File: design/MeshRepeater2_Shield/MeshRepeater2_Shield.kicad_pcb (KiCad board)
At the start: 2 copper layers, 90 x 60 mm, 5 parts

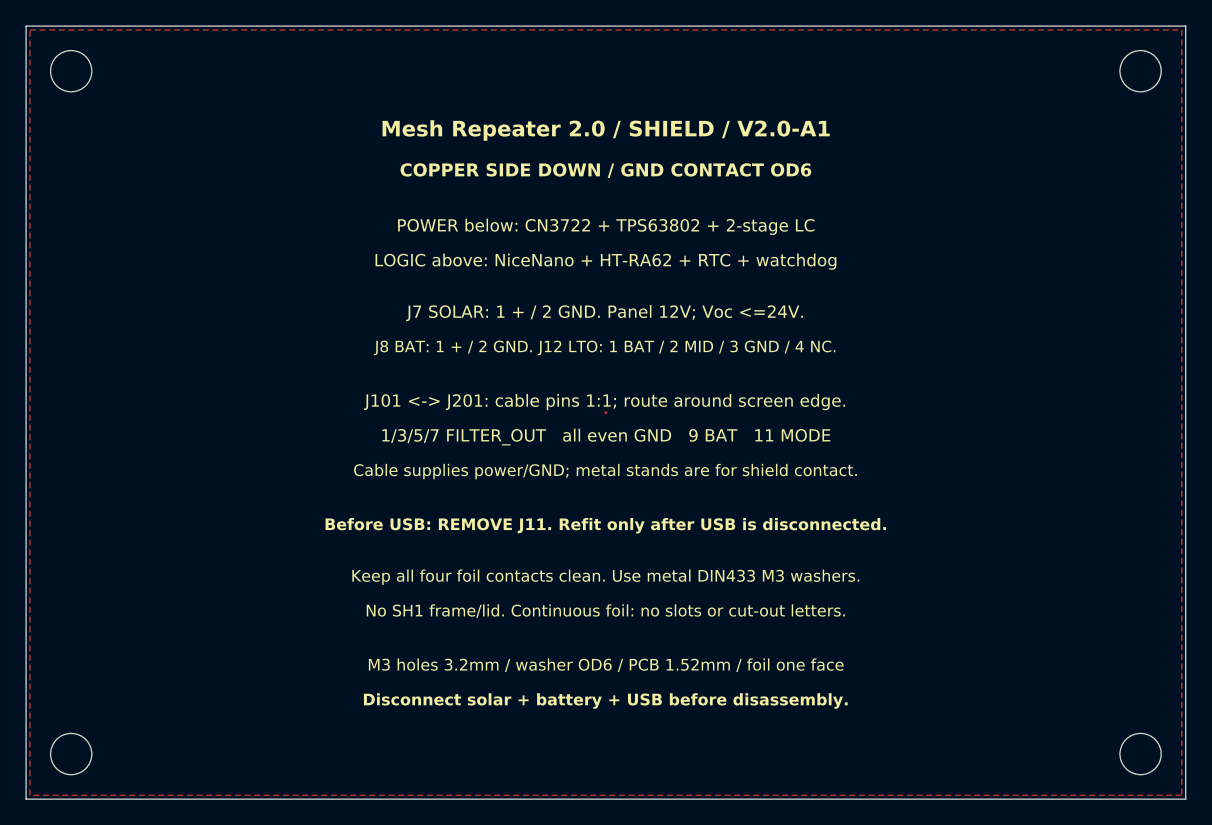
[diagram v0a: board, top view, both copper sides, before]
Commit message: Publish Mesh Repeater 2.0 A2
Add INA219 battery measurement with a 0.1 ohm shunt and vertical
12-pin interconnects through the middle shield. Publish updated
POWER, LOGIC and SHIELD KiCad sources, local models, BOM and A2
documentation with the completed routing and ground-via audit.

Preserve the V1 baseline and archives inside the V2 branch.
Validation: independent review 132/132; final artifact gate 499/499.
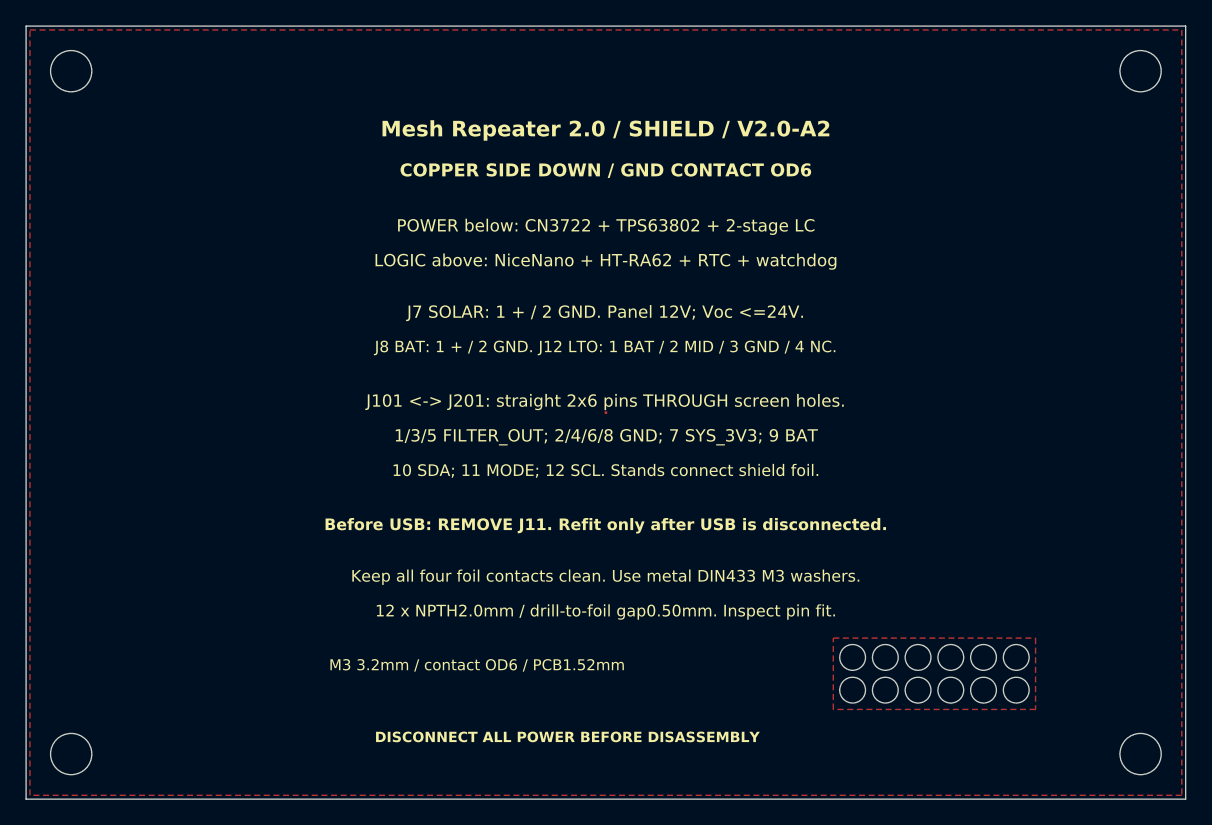
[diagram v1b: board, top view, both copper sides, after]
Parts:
- added HS1: INTERCONNECT PASS-THROUGH, Shield:Shield_Interconnect_2x06_NPTH_D2_CuVoid3, F.Cu at (64.2, 49.0)
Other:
- board text added: "1/3/5 FILTER_OUT; 2/4/6/8 GND; 7 SYS_3V3; 9 BAT"
- board text added: "10 SDA; 11 MODE; 12 SCL. Stands connect shield foil."
- board text added: "12 x NPTH2.0mm / drill-to-foil gap0.50mm. Inspect pin fit."
- board text added: "DISCONNECT ALL POWER BEFORE DISASSEMBLY"
- board text added: "J101 <-> J201: straight 2x6 pins THROUGH screen holes."
- board text added: "M3 3.2mm / contact OD6 / PCB1.52mm"
- board text added: "Mesh Repeater 2.0 / SHIELD / V2.0-A2"
- board text added: "Pin35mm / socket8.5mm / nominal engagement4.48mm."
- board text removed: "1/3/5/7 FILTER_OUT all even GND 9 BAT 11 MODE"
- board text removed: "Cable supplies power/GND; metal stands are for shield contact."
- board text removed: "Disconnect solar + battery + USB before disassembly."
- board text removed: "Full assembly instructions / cable / variants: project docs."
- board text removed: "J101 <-> J201: cable pins 1:1; route around screen edge."
- board text removed: "M3 holes 3.2mm / washer OD6 / PCB 1.52mm / foil one face"
- board text removed: "Mesh Repeater 2.0 / SHIELD / V2.0-A1"
- board text removed: "No SH1 frame/lid. Continuous foil: no slots or cut-out letters."
